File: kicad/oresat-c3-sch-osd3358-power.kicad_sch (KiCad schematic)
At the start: 37 parts, among them Q6 MMBT2907, U1 OSD3358-512M-BSM, U10 SN74AUC1G07DCKR, U14 TLVH431

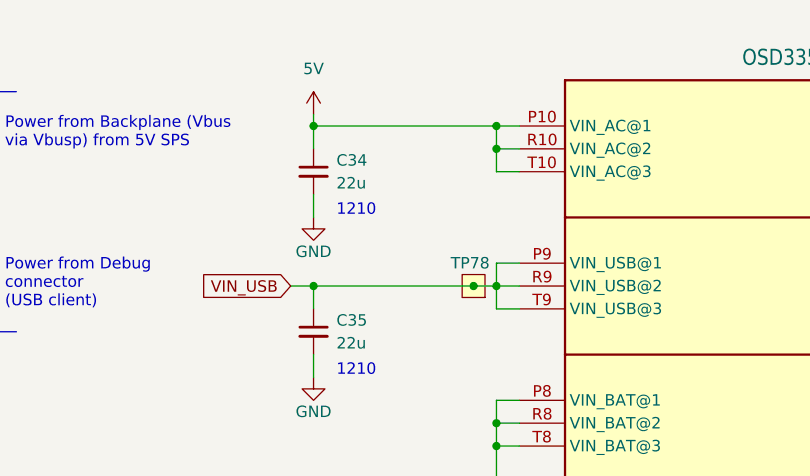
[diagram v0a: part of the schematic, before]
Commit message: Real part numbers for FB parts, routed signals for the UHF_ENABLE AND L_BAND_ENABLE signals.
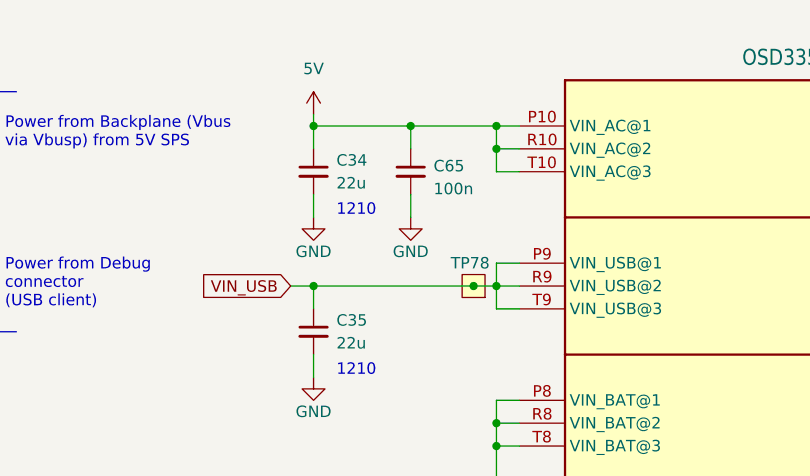
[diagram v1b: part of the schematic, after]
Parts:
- added C65: 100n, Capacitor_SMD:C_0603_1608Metric, symbol Device:C_Small
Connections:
- net 5V: now also C65.1
- net GND: now also C65.2
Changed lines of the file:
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@@
   (junction (at 265.43 104.14) (diameter 0) (color 0 0 0 0)
   )
+  (junction (at 177.165 53.34) (diameter 0) (color 0 0 0 0)
+  )
   (junction (at 298.45 132.08) (diameter 0) (color 0 0 0 0)
   )
@@
     (stroke (width 0) (type default))
   )
+  (wire (pts (xy 177.165 53.34) (xy 186.69 53.34))
+    (stroke (width 0) (type default))
+  )
   (wire (pts (xy 265.43 129.54) (xy 265.43 132.08))
     (stroke (width 0) (type default))
@@
     (stroke (width 0) (type default))
   )
+  (wire (pts (xy 177.165 55.88) (xy 177.165 53.34))
+    (stroke (width 0) (type default))
+  )
   (wire (pts (xy 265.43 185.42) (xy 265.43 182.88))
     (stroke (width 0) (type default))
@@
     (stroke (width 0) (type default))
   )
-  (wire (pts (xy 166.37 53.34) (xy 186.69 53.34))
+  (wire (pts (xy 166.37 53.34) (xy 177.165 53.34))
     (stroke (width 0) (type default))
   )
@@
   )
   (wire (pts (xy 308.61 149.86) (xy 298.45 149.86))
+    (stroke (width 0) (type default))
+  )
+  (wire (pts (xy 177.165 63.5) (xy 177.165 60.96))
     (stroke (width 0) (type default))
   )
@@
         (path "/65d12cdd-c326-4033-9053-c59fa4e0b25e/0c1da208-2d1c-4d05-9cc7-59584e50a6ac"
           (reference "R57") (unit 1)
+        )
+      )
+    )
+  )
+  (symbol (lib_id "Device:C_Small") (at 177.165 58.42 0) (unit 1)
+    (in_bom yes) (on_board yes) (dnp no) (fields_autoplaced)
+    (property "Reference" "C65" (at 179.705 57.7913 0)
+      (effects (font (size 1.27 1.27)) (justify left))
+    )
+    (property "Value" "100n" (at 179.705 60.3313 0)
+      (effects (font (size 1.27 1.27)) (justify left))
+    )
+    (property "Footprint" "Capacitor_SMD:C_0603_1608Metric" (at 177.165 58.42 0)
+      (effects (font (size 1.27 1.27)) hide)
+    )
+    (property "Datasheet" "~" (at 177.165 58.42 0)
+      (effects (font (size 1.27 1.27)) hide)
+    )
+    (pin "1")
+    (pin "2")
+    (instances
+      (project "oresat-c3"
+        (path "/65d12cdd-c326-4033-9053-c59fa4e0b25e/0c1da208-2d1c-4d05-9cc7-59584e50a6ac"
+          (reference "C65") (unit 1)
         )
       )
@@
         )
       )
+    )
+  )
+  (symbol (lib_id "power:GND") (at 177.165 63.5 0) (unit 1)
+    (in_bom yes) (on_board yes) (dnp no) (fields_autoplaced)
+    (property "Reference" "#PWR015" (at 177.165 69.85 0)
+      (effects (font (size 1.27 1.27)) hide)
+    )
+    (property "Value" "GND" (at 177.165 67.31 0)
+      (effects (font (size 1.27 1.27)))
+    )
+    (property "Footprint" "" (at 177.165 63.5 0)
+      (effects (font (size 1.27 1.27)) hide)
+    )
+    (property "Datasheet" "" (at 177.165 63.5 0)
+      (effects (font (size 1.27 1.27)) hide)
+    )
+    (pin "1")
+    (instances
+      (project "oresat-c3"
+        (path "/65d12cdd-c326-4033-9053-c59fa4e0b25e/0c1da208-2d1c-4d05-9cc7-59584e50a6ac"
+          (reference "#PWR015") (unit 1)
+        )
+      )

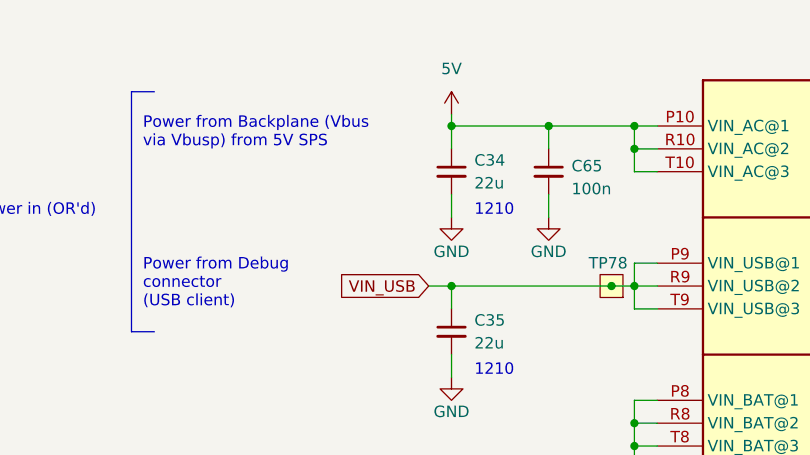
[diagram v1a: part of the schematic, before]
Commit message: Fixed some issues, including adding mrore capacitance. Also switched back to 0.38 mm for 50 ohm lines.
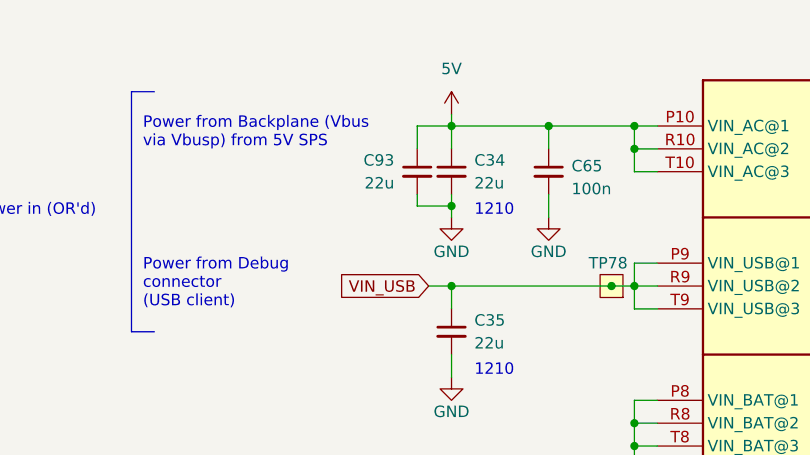
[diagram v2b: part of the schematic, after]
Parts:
- added C93: 22u, Capacitor_SMD:C_1210_3225Metric, symbol Device:C_Small
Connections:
- net 5V: now also C93.1
- net GND: now also C93.2
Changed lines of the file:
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@@
   (junction (at 265.43 71.12) (diameter 0) (color 0 0 0 0)
   )
+  (junction (at 166.37 62.23) (diameter 0) (color 0 0 0 0)
+  )
   (junction (at 285.75 53.34) (diameter 0) (color 0 0 0 0)
   )
@@
     (stroke (width 0) (type default))
   )
-  (wire (pts (xy 166.37 60.96) (xy 166.37 63.5))
+  (wire (pts (xy 166.37 60.96) (xy 166.37 62.23))
     (stroke (width 0) (type default))
   )
@@
     (stroke (width 0) (type default))
   )
+  (wire (pts (xy 162.56 53.34) (xy 166.37 53.34))
+    (stroke (width 0) (type default))
+  )
   (wire (pts (xy 260.35 132.08) (xy 265.43 132.08))
     (stroke (width 0) (type default))
@@
     (stroke (width 0) (type default))
   )
+  (wire (pts (xy 162.56 60.96) (xy 162.56 62.23))
+    (stroke (width 0) (type default))
+  )
   (polyline (pts (xy 130.81 49.53) (xy 130.81 76.2))
     (stroke (width 0) (type default))
@@
     (stroke (width 0) (type default))
   )
+  (wire (pts (xy 162.56 62.23) (xy 166.37 62.23))
+    (stroke (width 0) (type default))
+  )
   (wire (pts (xy 275.59 203.2) (xy 280.67 203.2))
     (stroke (width 0) (type default))
@@
     (stroke (width 0) (type default))
   )
+  (wire (pts (xy 162.56 55.88) (xy 162.56 53.34))
+    (stroke (width 0) (type default))
+  )
   (wire (pts (xy 186.69 182.88) (xy 186.69 185.42))
     (stroke (width 0) (type default))
@@
   )
   (wire (pts (xy 189.23 170.18) (xy 186.69 170.18))
+    (stroke (width 0) (type default))
+  )
+  (wire (pts (xy 166.37 62.23) (xy 166.37 63.5))
     (stroke (width 0) (type default))
   )
@@
         )
       )
+    )
+  )
+  (symbol (lib_id "Device:C_Small") (at 162.56 58.42 0) (mirror y) (unit 1)
+    (in_bom yes) (on_board yes) (dnp no)
+    (property "Reference" "C93" (at 160.02 57.1562 0)
+      (effects (font (size 1.27 1.27)) (justify left))
+    )
+    (property "Value" "22u" (at 160.02 59.6962 0)
+      (effects (font (size 1.27 1.27)) (justify left))
+    )
+    (property "Footprint" "Capacitor_SMD:C_1210_3225Metric" (at 162.56 58.42 0)
+      (effects (font (size 1.27 1.27)) hide)
+    )
+    (property "Datasheet" "~" (at 162.56 58.42 0)
+      (effects (font (size 1.27 1.27)) hide)
+    )
+    (pin "1")
+    (pin "2")
+    (instances
+      (project "oresat-c3"
+        (path "/65d12cdd-c326-4033-9053-c59fa4e0b25e/0c1da208-2d1c-4d05-9cc7-59584e50a6ac"
+          (reference "C93") (unit 1)
+        )
+      )

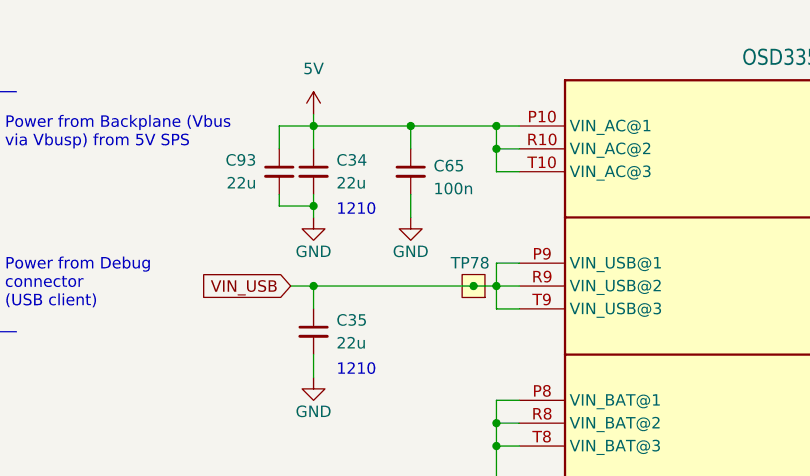
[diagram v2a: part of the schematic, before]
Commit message: Last changes to 6.1 after design review today.
Added logo.
Brought up to KiCAD 8.0.1.
Added text next to smpm connectors.
Fixed some 0.127 traces that didn't need to be that thin on nRESET.
Fix silkscreen refdeses on new components.
Move pin 1 marker on the BP0805A1308.
Remove thermals on PA bottom layer.
Added oresat-c3-eagle-import symbols and footprints so everything is local.
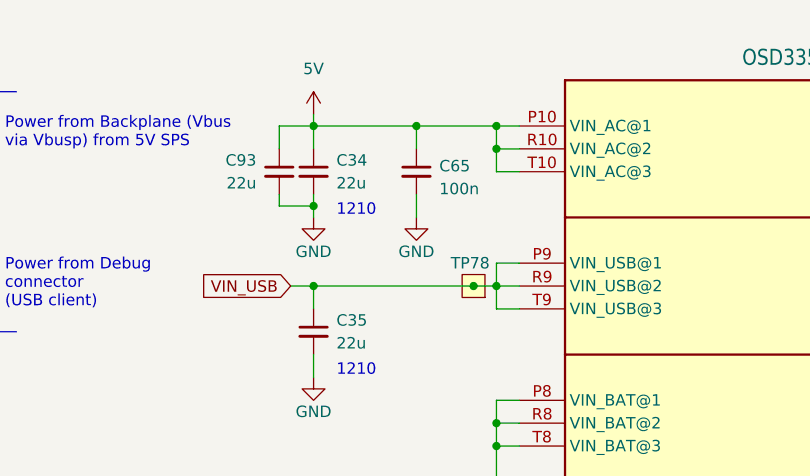
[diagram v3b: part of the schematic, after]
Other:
- moved on the sheet: C65

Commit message: BOM cleanups; modified test points to not show up on BOMs, fixed some minor BOM shenaigans (3k vs 3.0k), and imported into the board.
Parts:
- TP127, TP128, TP129, TP130, TP131, TP132, TP133, TP135, TP73, TP74, TP75, TP76, TP77, TP78, TP79, TP80, TP81, TP82, TP83, TP84, TP85: now left out of the parts list
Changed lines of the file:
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@@
 		(at 265.43 147.32 270)
 		(unit 1)
-		(exclude_from_sim no)
-		(in_bom yes)
+		(exclude_from_sim yes)
+		(in_bom no)
 		(on_board yes)
 		(dnp no)
@@
 			)
 		)
-		(property "Description" ""
+		(property "Description" "0.75 mm TH test point; good for scope probes and jumpers"
 			(at 265.43 147.32 0)
 			(effects
@@
 		(at 265.43 170.18 270)
 		(unit 1)
-		(exclude_from_sim no)
-		(in_bom yes)
+		(exclude_from_sim yes)
+		(in_bom no)
 		(on_board yes)
 		(dnp no)
@@
 			)
 		)
-		(property "Description" ""
+		(property "Description" "0.75 mm TH test point; good for scope probes and jumpers"
 			(at 265.43 170.18 0)
 			(effects
@@
 		(at 170.18 205.74 180)
 		(unit 1)
-		(exclude_from_sim no)
-		(in_bom yes)
+		(exclude_from_sim yes)
+		(in_bom no)
 		(on_board yes)
 		(dnp no)
@@
 			)
 		)
-		(property "Description" ""
+		(property "Description" "0.75 mm TH test point; good for scope probes and jumpers"
 			(at 170.18 205.74 0)
 			(effects
@@
 		(at 186.69 149.86 180)
 		(unit 1)
-		(exclude_from_sim no)
-		(in_bom yes)
+		(exclude_from_sim yes)
+		(in_bom no)
 		(on_board yes)
 		(dnp no)
@@
 			)
 		)
-		(property "Description" ""
+		(property "Description" "1mm round SMT test point"
 			(at 186.69 149.86 0)
 			(effects
@@
 		(at 292.1 215.9 180)
 		(unit 1)
-		(exclude_from_sim no)
-		(in_bom yes)
+		(exclude_from_sim yes)
+		(in_bom no)
 		(on_board yes)
 		(dnp no)
@@
 			)
 		)
-		(property "Description" ""
+		(property "Description" "0.75 mm TH test point; good for scope probes and jumpers"
 			(at 292.1 215.9 0)
 			(effects
@@
 		(at 265.43 71.12 270)
 		(unit 1)
-		(exclude_from_sim no)
-		(in_bom yes)
+		(exclude_from_sim yes)
+		(in_bom no)
 		(on_board yes)
 		(dnp no)
@@
 			)
 		)
-		(property "Description" ""
+		(property "Description" "0.75 mm TH test point; good for scope probes and jumpers"
 			(at 265.43 71.12 0)
 			(effects
@@
 		(at 186.69 172.72 180)
 		(unit 1)
-		(exclude_from_sim no)
-		(in_bom yes)
+		(exclude_from_sim yes)
+		(in_bom no)
 		(on_board yes)
 		(dnp no)
@@
 			)
 		)
-		(property "Description" ""
+		(property "Description" "1mm round SMT test point"
 			(at 186.69 172.72 0)
 			(effects
@@
 		(at 184.15 71.12 180)
 		(unit 1)
-		(exclude_from_sim no)
-		(in_bom yes)
+		(exclude_from_sim yes)
+		(in_bom no)
 		(on_board yes)
 		(dnp no)
@@
 			)
 		)
-		(property "Description" ""
+		(property "Description" "0.75 mm TH test point; good for scope probes and jumpers"
 			(at 184.15 71.12 0)
 			(effects
@@
 		(at 170.18 212.09 180)
 		(unit 1)
-		(exclude_from_sim no)
-		(in_bom yes)
+		(exclude_from_sim yes)
+		(in_bom no)
 		(on_board yes)
 		(dnp no)
@@
 			)
 		)
-		(property "Description" ""
+		(property "Description" "0.75 mm TH test point; good for scope probes and jumpers"
 			(at 170.18 212.09 0)
 			(effects
@@
 		(at 170.18 193.04 180)
 		(unit 1)
-		(exclude_from_sim no)
-		(in_bom yes)
+		(exclude_from_sim yes)
+		(in_bom no)
 		(on_board yes)
 		(dnp no)
@@
 			)
 		)
-		(property "Description" ""
+		(property "Description" "0.75 mm TH test point; good for scope probes and jumpers"
 			(at 170.18 193.04 0)
 			(effects
@@
 		(at 186.69 157.48 180)
 		(unit 1)
-		(exclude_from_sim no)
-		(in_bom yes)
+		(exclude_from_sim yes)
+		(in_bom no)
 		(on_board yes)
 		(dnp no)
@@
 			)
 		)
-		(property "Description" ""
+		(property "Description" "1mm round SMT test point"
 			(at 186.69 157.48 0)
 			(effects
@@
 		(at 265.43 53.34 270)
 		(unit 1)
-		(exclude_from_sim no)
-		(in_bom yes)
+		(exclude_from_sim yes)
+		(in_bom no)
 		(on_board yes)
 		(dnp no)
@@
 			)
 		)
-		(property "Description" ""
+		(property "Description" "0.75 mm TH test point; good for scope probes and jumpers"
 			(at 265.43 53.34 0)
 			(effects
@@
 		(at 170.18 185.42 180)
 		(unit 1)
-		(exclude_from_sim no)
-		(in_bom yes)
+		(exclude_from_sim yes)
+		(in_bom no)
 		(on_board yes)
 		(dnp no)
@@
 			)
 		)
-		(property "Description" ""
+		(property "Description" "0.75 mm TH test point; good for scope probes and jumpers"
 			(at 170.18 185.42 0)
 			(effects
@@
 		(at 265.43 101.6 270)
 		(unit 1)
-		(exclude_from_sim no)
-		(in_bom yes)
+		(exclude_from_sim yes)
+		(in_bom no)
 		(on_board yes)
 		(dnp no)
@@
 			)
 		)
-		(property "Description" ""
+		(property "Description" "0.75 mm TH test point; good for scope probes and jumpers"
 			(at 265.43 101.6 0)
 			(effects
@@
 		(at 186.69 137.16 180)
 		(unit 1)
-		(exclude_from_sim no)
-		(in_bom yes)
+		(exclude_from_sim yes)
+		(in_bom no)
 		(on_board yes)
 		(dnp no)
@@
 			)
 		)
-		(property "Description" ""
+		(property "Description" "1mm round SMT test point"
 			(at 186.69 137.16 0)
 			(effects
@@
 		(at 265.43 88.9 270)
 		(unit 1)
-		(exclude_from_sim no)
-		(in_bom yes)
+		(exclude_from_sim yes)
+		(in_bom no)
 		(on_board yes)
 		(dnp no)
@@
 			)
 		)
-		(property "Description" ""
+		(property "Description" "0.75 mm TH test point; good for scope probes and jumpers"
 			(at 265.43 88.9 0)
 			(effects
@@
 		(at 186.69 127 180)
 		(unit 1)
-		(exclude_from_sim no)
-		(in_bom yes)
+		(exclude_from_sim yes)
+		(in_bom no)
 		(on_board yes)
 		(dnp no)
@@
 			)
 		)
-		(property "Description" ""
+		(property "Description" "1mm round SMT test point"
 			(at 186.69 127 0)
 			(effects
@@
 		(at 186.69 96.52 180)
 		(unit 1)
-		(exclude_from_sim no)
-		(in_bom yes)
+		(exclude_from_sim yes)
+		(in_bom no)
 		(on_board yes)
 		(dnp no)
@@
 			)
 		)
-		(property "Description" ""
+		(property "Description" "1mm round SMT test point"
 			(at 186.69 96.52 0)
 			(effects
@@
 		(at 186.69 93.98 180)
 		(unit 1)
-		(exclude_from_sim no)
-		(in_bom yes)
+		(exclude_from_sim yes)
+		(in_bom no)
 		(on_board yes)
 		(dnp no)
@@
 			)
 		)
-		(property "Description" ""
+		(property "Description" "1mm round SMT test point"
 			(at 186.69 93.98 0)
 			(effects
@@
 		(at 275.59 203.2 180)
 		(unit 1)
-		(exclude_from_sim no)
-		(in_bom yes)
+		(exclude_from_sim yes)
+		(in_bom no)
 		(on_board yes)
 		(dnp no)
@@
 			)
 		)
-		(property "Description" ""
+		(property "Description" "1mm round SMT test point"
 			(at 275.59 203.2 0)
 			(effects
@@
 		(at 186.69 165.1 180)
 		(unit 1)
-		(exclude_from_sim no)
-		(in_bom yes)
+		(exclude_from_sim yes)
+		(in_bom no)
 		(on_board yes)
 		(dnp no)
@@
 			)
 		)
-		(property "Description" ""
+		(property "Description" "1mm round SMT test point"
 			(at 186.69 165.1 0)
 			(effects

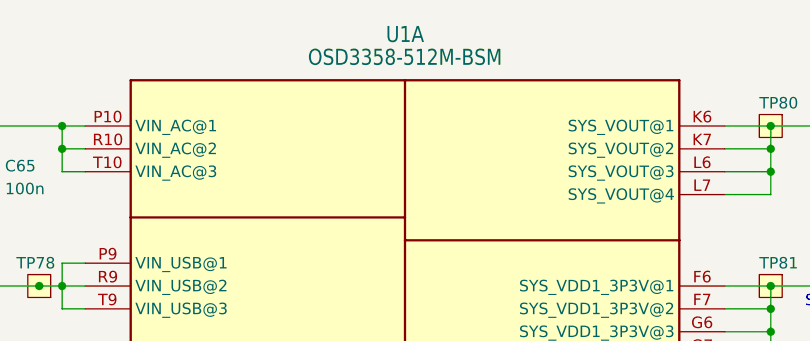
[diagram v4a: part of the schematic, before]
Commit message: Fixed more part numbers while in process of doing BOM inventory, including eMMC and FRAM.
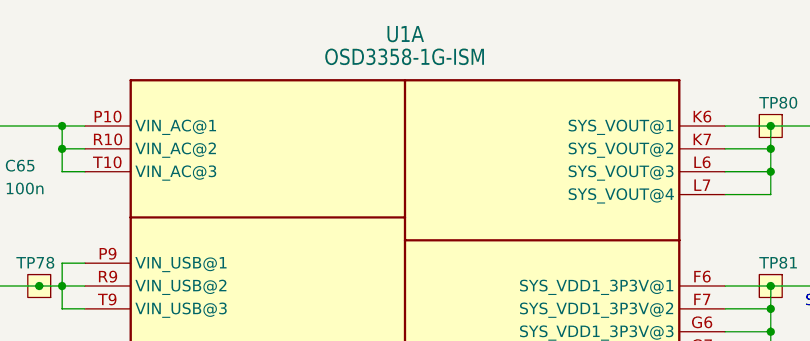
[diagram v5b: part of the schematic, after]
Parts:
- U1: value OSD3358-512M-BSM -> OSD3358-1G-ISM
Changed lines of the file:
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@@
 			)
 		)
-		(property "Value" "OSD3358-512M-BSM"
+		(property "Value" "OSD3358-1G-ISM"
 			(at 224.79 45.72 0)
 			(effects

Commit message: Added MFR, MPN, Description, DST, and DPN to all components using the amazing KiCAD table properties editor. Yay KiCAD. Attemping to make the BOM be self-assembling.
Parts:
- C33, C65, C78: DPN (none) -> 587-3472-1-ND; DST (none) -> Digi-Key; MFR (none) -> Taiyo Yuden; MPN (none) -> TMK107BJ104KAHT
- C34, C35, C36, C93: DPN (none) -> 490-GCM32EC71E226KE36KCT-ND; DST (none) -> Digi-Key; MFR (none) -> Murata Electronics; MPN (none) -> GCM32EC71E226KE36K
- D8: DPN (none) -> 732-4971-1-ND; DST (none) -> Digi-Key; MFR (none) -> Wurth; MPN (none) -> 150060GS75000
- Q6: DPN (none) -> 1727-1884-1-ND; DST (none) -> Digi-Key; MFR (none) -> Nexperia; MPN (none) -> PMBT2907A,235
- R50, R53, R54, R57: DPN (none) -> RMCF0603FT10K0CT-ND; DST (none) -> Digi-Key; MFR (none) -> Stackpole Electronics Inc; MPN (none) -> RMCF0603FT10K0
- R55: DPN (none) -> RMCF0603FT499RCT-ND; DST (none) -> Digi-Key; MFR (none) -> Stackpole Electronics Inc; MPN (none) -> RMCF0603FT499R
- R56: DPN (none) -> RMCF0603FT40K2CT-ND; DST (none) -> Digi-Key; MFR (none) -> Stackpole Electronics Inc; MPN (none) -> RMCF0603FT40K2
- U1: DPN (none) -> 1676-OSD3358-1G-ISM-ND; DST (none) -> Digi-Key; Distributor DigiKey -> (none); MFR (none) -> Octavo Systems; MPN OSD3358-512M-BSM -> OSD3358-1G-ISM
- U10: DPN (none) -> 296-12464-1-ND; DST (none) -> Digi-Key; MFR (none) -> Texas Instruments; MPN (none) -> SN74AUC1G07DCKR
- U14: DPN (none) -> 296-17979-1-ND; DST (none) -> Digi-Key; MFR (none) -> Texas Instruments; MPN (none) -> TLVH431BCDBZT

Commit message: C3 v6.1 release
Updated to KiCad 9.0.6. Updated to version 6.1; there are small changes that have been lost in time. Lots of new ERC and DRC errors that need to be cleaned up.
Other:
- company: (none) -> Portland State Aerospace Society
- title: OreSat C3: OSD3358: SIP A -> OreSat C3 Card
